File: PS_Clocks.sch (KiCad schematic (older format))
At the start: 50 parts, among them IC16 TCA9548ARGER, J12 Conn_01x03, Q17 DMN26D0UFB4-7, U21 SI5332B-D-GM1, U22 570BAB001614DGR, U3 570BAB001614DGR, Y3 27MHz

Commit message: Update May --> See Update Note
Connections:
- net CLK_GEN_SCLK: now also IC16.2 (SC0), R135.2; no longer IC16.4 (SC1), R139.2
- net CLK_GEN_SDA: now also IC16.1 (SD0), R133.2; no longer IC16.3 (SD1), R137.2
- net USER_SI570_SCL: now also IC16.4 (SC1), R139.2; no longer IC16.2 (SC0), R135.2
- net USER_SI570_SDA: now also IC16.3 (SD1), R137.2; no longer IC16.1 (SD0), R133.2
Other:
- note added: "User Clk for Kria 200MHz for MIPI DPHY"
- note removed: "User Clk for Kria (80MHz to 800MHz)"
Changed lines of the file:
@@
 $EndComp
 Text Notes 10665 1885 0    157  ~ 0
-User Clk for Kria (80MHz to 800MHz)
+User Clk for Kria 200MHz for MIPI DPHY
 Text HLabel 13600 3375 2    50   Output ~ 0
 USER_SI570_HPA_CLK0_N
@@
 Wire Wire Line
 	4700 3900 5300 3900
+Text Label 1825 9355 0    50   ~ 0
+USER_SI570_SCL
+Text Label 1825 9255 0    50   ~ 0
+USER_SI570_SDA
+Text Label 1825 9055 0    50   ~ 0
+CLK_GEN_SDA
 Text Label 1825 9155 0    50   ~ 0
-USER_SI570_SCL
-Text Label 1825 9055 0    50   ~ 0
-USER_SI570_SDA
-Text Label 1825 9255 0    50   ~ 0
-CLK_GEN_SDA
-Text Label 1825 9355 0    50   ~ 0
 CLK_GEN_SCLK
 Wire Wire Line

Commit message: Pre-Production Push
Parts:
- removed U22: 570BAB001614DGR, ApotheoTech_CXP_Lib:570BAB001614DGR, symbol ApotheoTech:570BAB001614DGR
- added R47, R48, R49: DNP, Resistor_SMD:R_0402_1005Metric, symbol Device:R
- added U7: SG5032VAN, ApotheoTech_CXP_Lib:SG5032_5mm_3_2mm, symbol ApotheoTech:SG5032VAN
- R129: value 10K -> DNP; DNP_Val (none) -> 10k
- R149, R150: value 10K -> 2.21k; PartNumber ERJ-2RKF1002X -> ERJ-2RKF2211X; URL https://www.digikey.com/en/products/detail/panasonic-electronic-components/ERJ-2RKF1002X/192073 -> https://www.digikey.com/en/products/detail/panasonic-electronic-components/ERJ-2RKF2211X/192198
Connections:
- net GND: now also R48.2, R49.2, U7.3 (GND)
- net USER_SI570_HPA_CLK0_N: now also U7.5 (~OUT)
- net USER_SI570_HPA_CLK0_P: now also U7.4 (OUT)
- net UTIL_3V3: now also R47.1, U7.6 (VCC)
- net at R131.2: now also U7.1 (OE)
- net at U3.1 (NC): now also R47.2, R48.1
- net at R10.2, U3.2 (OE): now also R49.1
- net GTH_REFCLK1_N renamed GTH_REFCLK0_C2M_N
- net GTH_REFCLK1_P renamed GTH_REFCLK0_C2M_P
- no-connect marks 7 -> 8
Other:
- note added: "Added DNP in case we run into part shortages"
- moved on the sheet: C175, R131

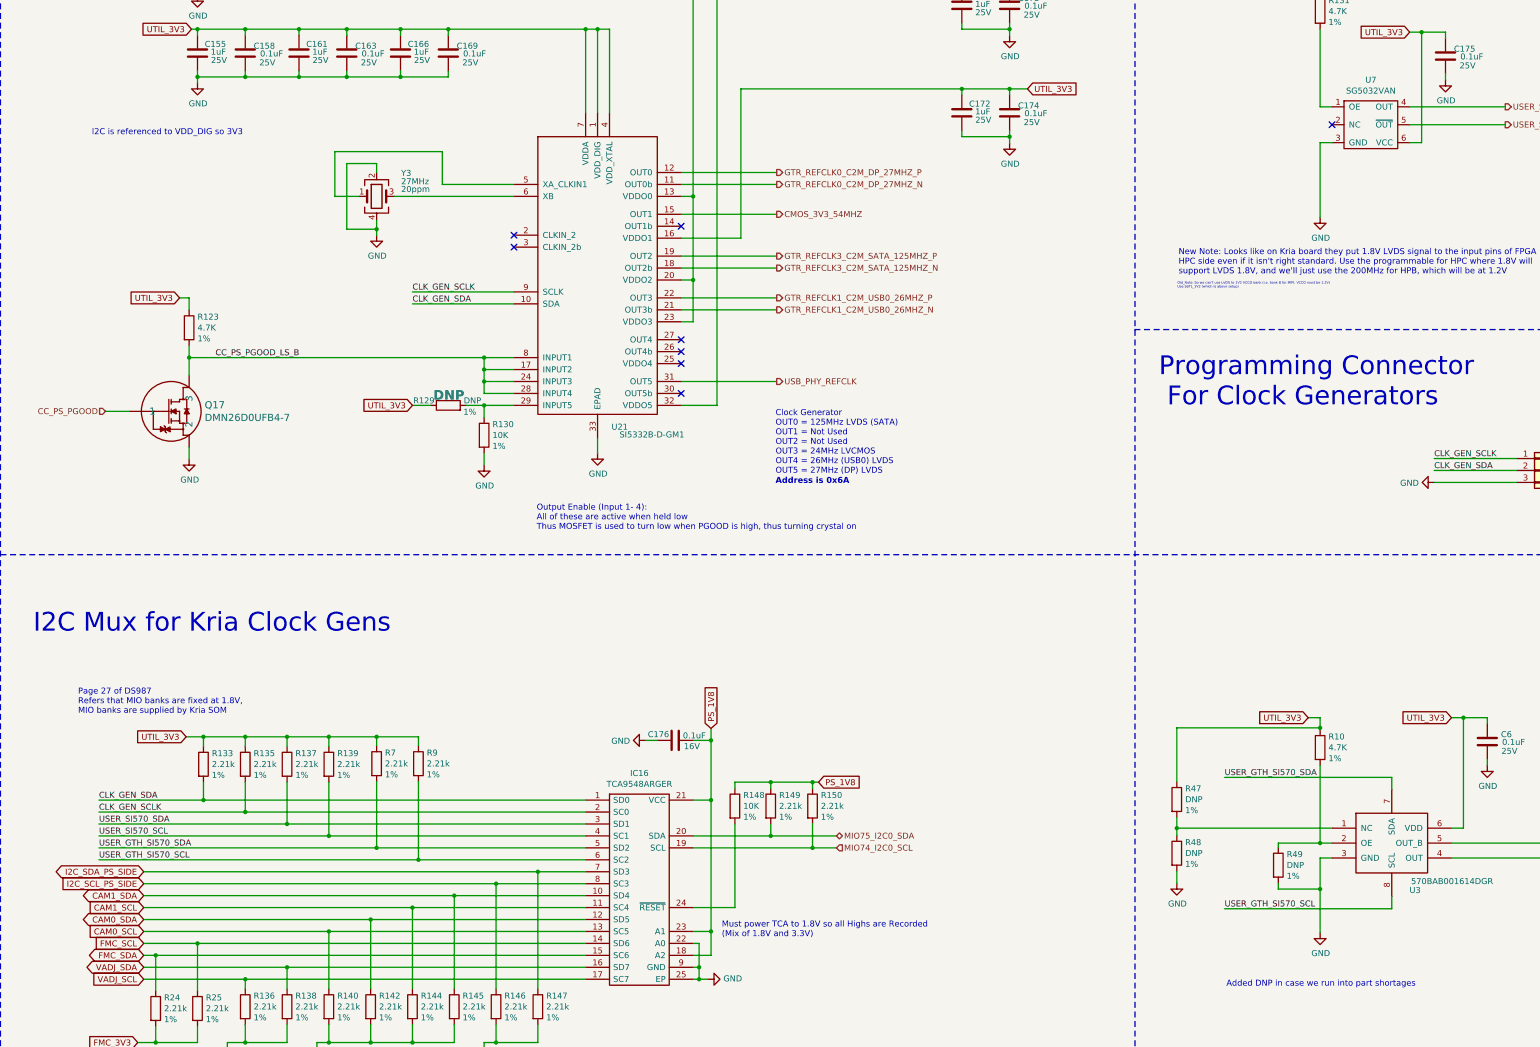
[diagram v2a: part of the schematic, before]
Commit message: Update to Kicad 7
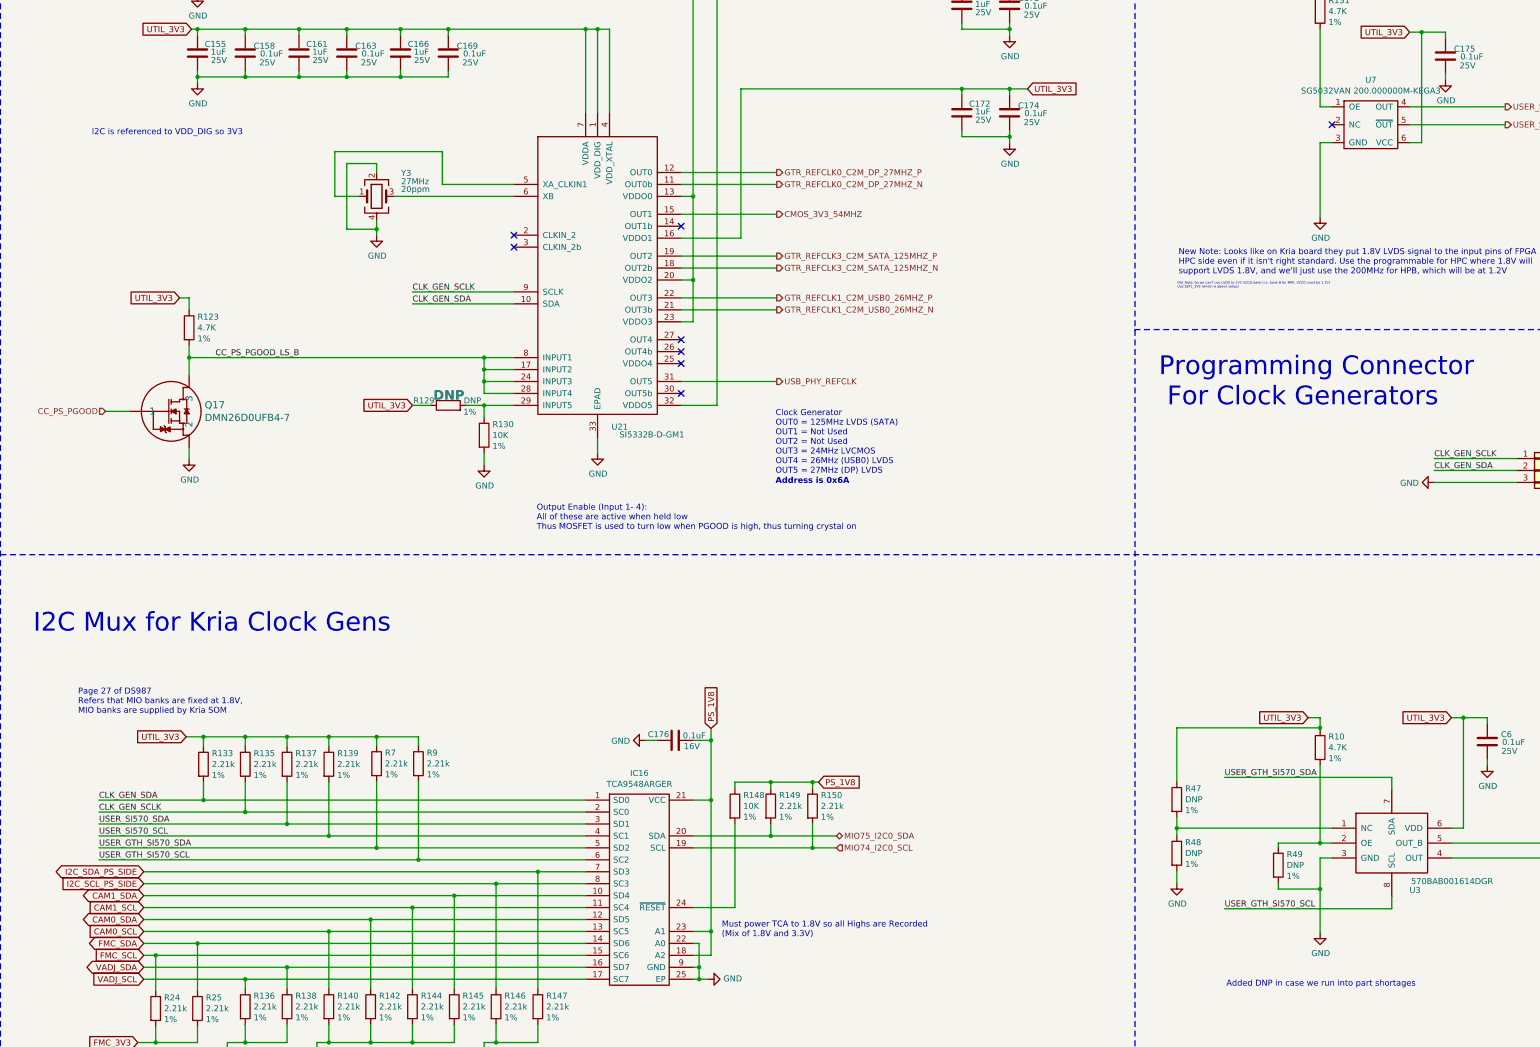
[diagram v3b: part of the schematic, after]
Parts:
- U7: value SG5032VAN -> SG5032VAN 200.000000M-KEGA3; Alt (none) -> ECX-L35CN-200.000-TR; URL (none) -> https://www.mouser.com/ProductDetail/ECS/ECX-L35CN-200.000-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
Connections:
- net FMC_SCL: now also IC16.15 (SC6), R24.1; no longer IC16.14 (SD6), R25.1
- net FMC_SDA: now also IC16.14 (SD6), R25.1; no longer IC16.15 (SC6), R24.1
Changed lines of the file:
@@
 Wire Wire Line
 	4500 9555 5900 9555
-Text GLabel 2200 10255 0    50   Input ~ 0
+Text GLabel 2200 10355 0    50   Input ~ 0
 FMC_SCL
-Text GLabel 2200 10355 0    50   BiDi ~ 0
+Text GLabel 2200 10255 0    50   BiDi ~ 0
 FMC_SDA
 Text GLabel 2200 10555 0    50   Input ~ 0
@@
 P 12500 3400
 F 0 "U7" H 12475 3775 50  0000 C CNN
-F 1 "SG5032VAN" H 12475 3684 50  0000 C CNN
+F 1 "SG5032VAN 200.000000M-KEGA3 " H 12475 3684 50  0000 C CNN
 F 2 "ApotheoTech_CXP_Lib:SG5032_5mm_3_2mm" H 12500 3400 50  0001 C CNN
 F 3 "" H 12500 3400 50  0001 C CNN
+F 4 "ECX-L35CN-200.000-TR " H 12500 3400 50  0001 C CNN "Alt"
+F 5 "https://www.mouser.com/ProductDetail/ECS/ECX-L35CN-200.000-TR?qs=vvQtp7zwQdORW0voyIBaMQ%3D%3D" H 12500 3400 50  0001 C CNN "URL"
 	1    12500 3400
 	1    0    0    -1
